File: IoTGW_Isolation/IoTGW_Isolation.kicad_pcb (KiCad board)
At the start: 4 copper layers, 40 x 48.5 mm, 33 parts, among them J1 39502-1009, J2 39502-1009, U1 TEA1-0505, U2 ISO1452BDWR, U3 LTV-817S, U4 LTV-817S, U5 LTV-817S, U6 LTV-817S, U7 LTV-817S, U8 LTV-817S

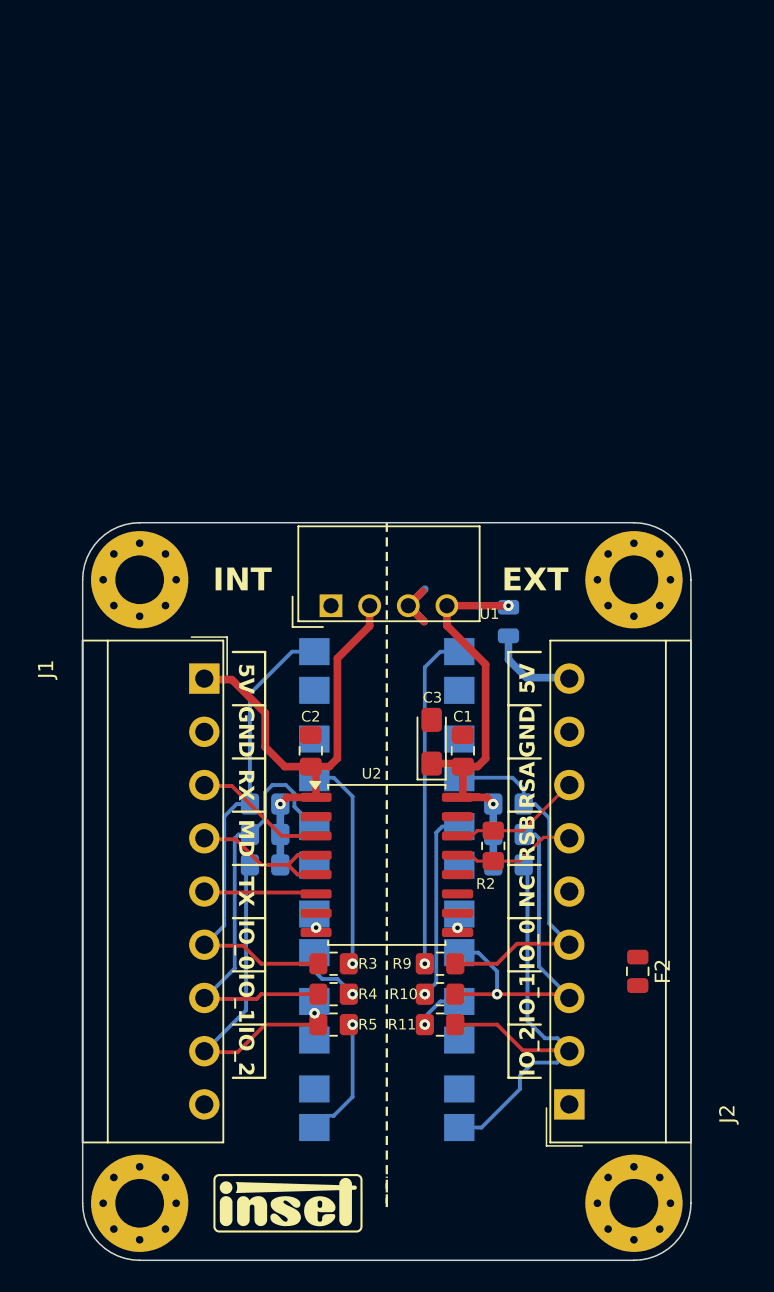
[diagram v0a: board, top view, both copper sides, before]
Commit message: 3,3V logic update
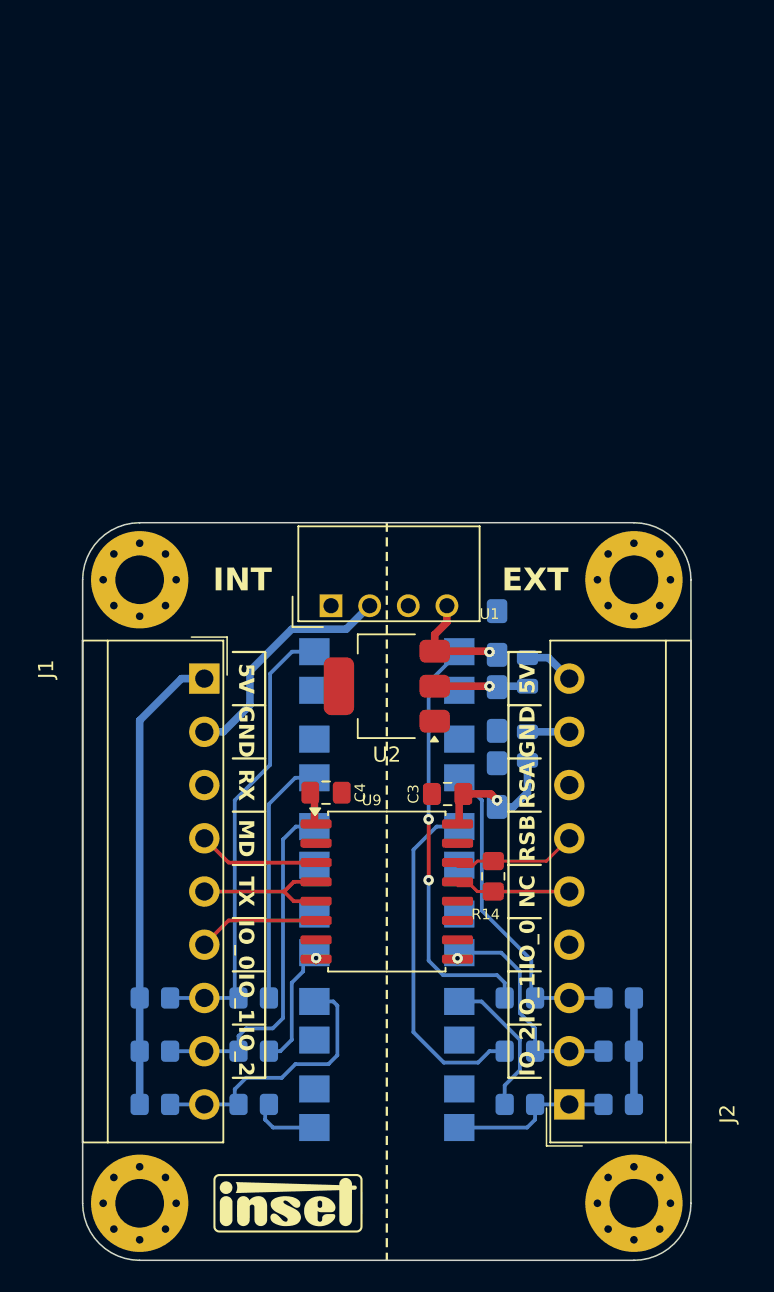
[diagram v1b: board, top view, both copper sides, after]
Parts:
- added C1: 10uF, Capacitor_Tantalum_SMD:CP_EIA-3216-18_Kemet-A_Pad1.58x1.35mm_HandSolder, B.Cu at (152.2, 97.2)
- added C2: 10uF, Capacitor_Tantalum_SMD:CP_EIA-3216-18_Kemet-A_Pad1.58x1.35mm_HandSolder, B.Cu at (152.2, 102.2)
- added U2: NCP1117-3.3, Package_TO_SOT_SMD:SOT-223-3_TabPin2, F.Cu at (145.0, 100.8)
- C5: renamed from C3; moved to B.Cu
- F2: moved to B.Cu
- R10: renamed from R11; moved to B.Cu
- R2: renamed from R3; moved to B.Cu
- R3: renamed from R4; moved to B.Cu
- R4: renamed from R5; moved to B.Cu
- R8: renamed from R9; moved to B.Cu
- R9: renamed from R10; moved to B.Cu
- moved R13 17.3 mm to (129.8, 128.2), turned to 180 degrees
- moved R7 17.3 mm to (160.2, 128.2), turned to 0 degrees
- moved F2 16.5 mm to (154.2, 104.7), turned to 90 degrees
- moved R12 16.0 mm to (129.8, 124.8), turned to 180 degrees
- moved R6 16.0 mm to (160.2, 124.8), turned to 0 degrees
- moved R11 14.7 mm to (129.8, 121.2), turned to 180 degrees
- moved R5 14.7 mm to (160.2, 121.2), turned to 0 degrees
- moved R10 7.42 mm to (153.8, 128.2)
- moved R4 7.42 mm to (136.2, 128.2)
- moved R3 6.45 mm to (136.2, 124.8)
- moved R9 6.45 mm to (153.8, 124.8)
- moved R2 5.71 mm to (136.2, 121.2)
- moved R8 5.71 mm to (153.8, 121.2)
- moved C5 5.16 mm to (152.2, 107.2)
- moved F1 3.54 mm to (154.2, 99.8), turned to 90 degrees
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- renumbered C1 to C3, C2 to C4, R12 to R11, R13 to R12, R14 to R13, R2 to R14, R6 to R5, R7 to R6, R8 to R7, U2 to U9
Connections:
- C4 pad 1: +5V -> +3.3V
- F1 pad 1: +5V_OUT -> +3.3V_OUT
- F1 pad 2: 5V_CONN -> 3.3V_CONN
- J2 pad 1: 3.3V_CONN -> GPIO_EXT_2
- J2 pad 2: 5V_CONN -> GPIO_EXT_1
- J2 pad 3: GND_OUT -> GPIO_EXT_0
- J2 pad 4: RS-485_+ -> unconnected-(J2-Pin_4-Pad4)
- J2 pad 6: unconnected-(J2-Pin_6-Pad6) -> RS-485_+
- J2 pad 7: GPIO_EXT_0 -> GND_OUT
- J2 pad 8: GPIO_EXT_1 -> 5V_CONN
- J2 pad 9: GPIO_EXT_2 -> 3.3V_CONN
- R11 pad 2: +5V -> +3.3V
- R12 pad 2: +5V -> +3.3V
- R13 pad 2: +5V -> +3.3V
- R5 pad 2: +5V_OUT -> +3.3V_OUT
- R6 pad 2: +5V_OUT -> +3.3V_OUT
- R7 pad 2: +5V_OUT -> +3.3V_OUT
- U9 pad 1: +5V -> +3.3V
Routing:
- net +3.3V: track 0.00 -> 32.6 mm
- net GPIO_EXT_2: track 32.0 -> 10.7 mm
- net +5V: track 32.3 -> 15.6 mm, vias 1 -> 0
- net +3.3V_OUT: track 0.00 -> 13.1 mm, vias 0 -> 1
- net +5V_OUT: track 28.6 -> 16.0 mm
- net Net-(R9-Pad1): track 12.6 -> 22.8 mm, vias 1 -> 0
- net GPIO_EXT_1: track 24.2 -> 14.7 mm, vias 1 -> 0
- net Net-(R10-Pad1): track 3.19 -> 9.69 mm, vias 1 -> 0
- net GPIO_OPTO_1: track 28.6 -> 22.6 mm
- net GND_OUT: track 6.15 -> 0.31 mm
- net Net-(R8-Pad1): track 22.2 -> 27.8 mm, vias 1 -> 2
- net GPIO_OPTO_2: track 22.3 -> 17.8 mm, vias 1 -> 0
- net Net-(R4-Pad1): track 8.10 -> 4.20 mm, vias 1 -> 0
- net Net-(R3-Pad1): track 4.36 -> 8.16 mm, vias 1 -> 0
- net 3.3V_CONN: track 0.00 -> 3.32 mm
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
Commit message: 3v3 update
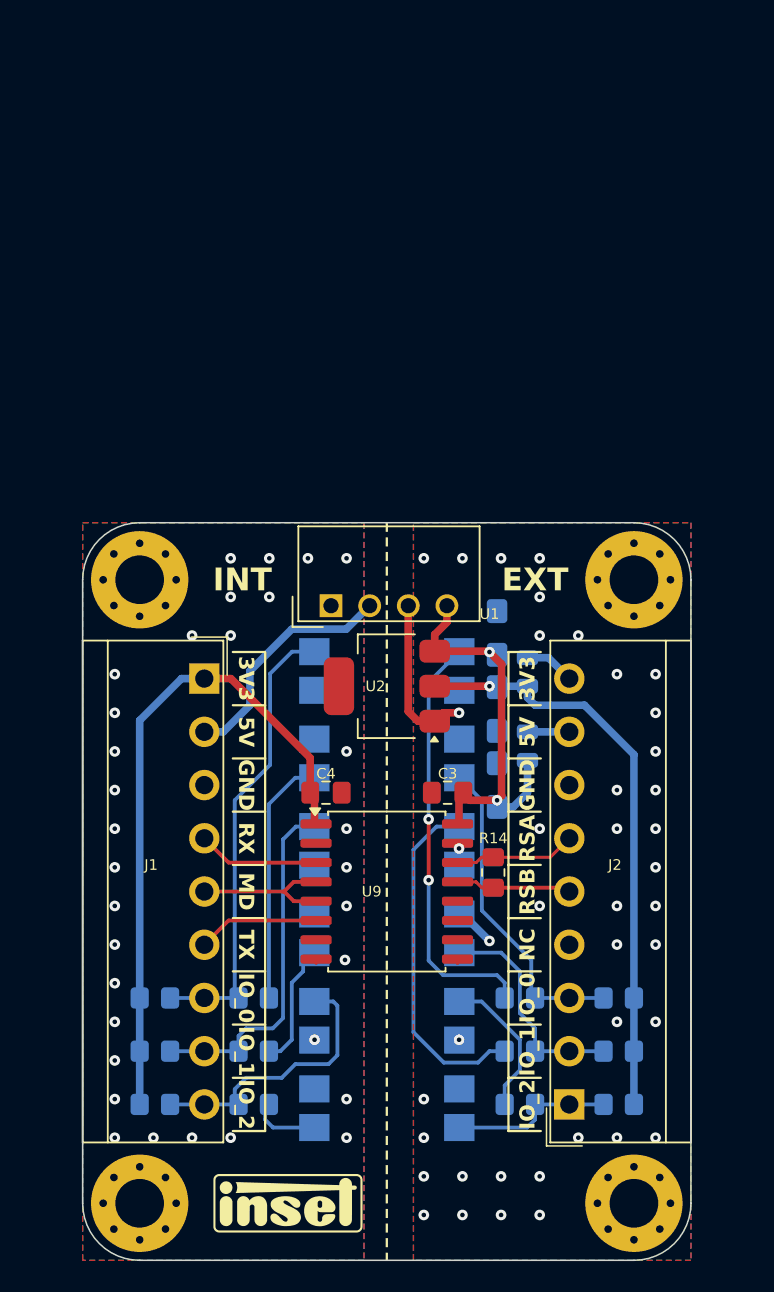
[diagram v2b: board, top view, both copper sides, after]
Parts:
- moved R14 0.25 mm to (152.0, 113.0)
- moved C3 0.09 mm to (149.0, 107.8)
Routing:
- net +3.3V_OUT: track 13.1 -> 38.4 mm
- net GND_OUT: track 0.31 -> 15.0 mm, vias 1 -> 41
- net +3.3V: track 32.6 -> 44.0 mm
- net +5V_OUT: track 16.0 -> 26.2 mm
- net GND: track 0.32 -> 0.28 mm, vias 1 -> 32
- added copper zone on B.Cu, net GND
- added copper zone on F.Cu, net GND
- added copper zone on B.Cu, net GND_OUT
- added copper zone on F.Cu, net GND_OUT
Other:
- board text added: "3V3"

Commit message: bom update
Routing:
- net GND_OUT: vias 41 -> 4
- net GND: vias 32 -> 2

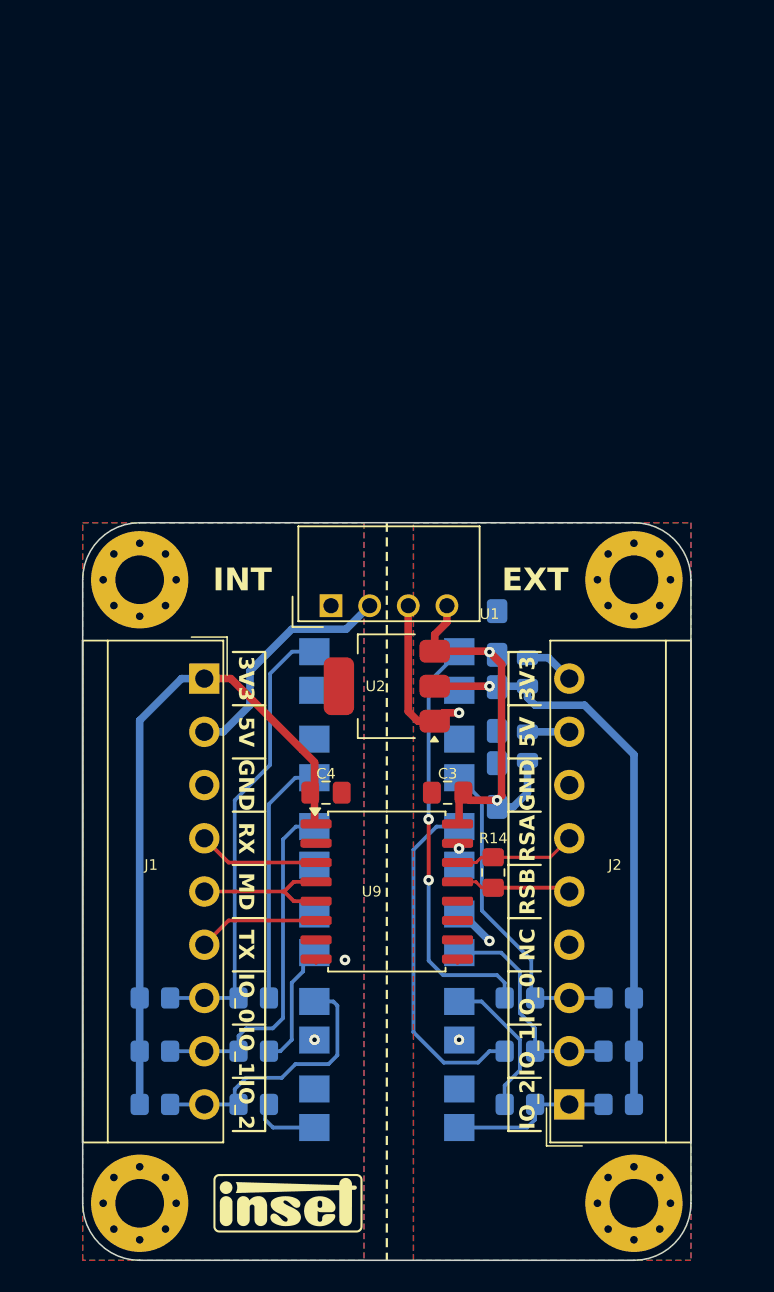
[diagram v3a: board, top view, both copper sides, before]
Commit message: FInal PCB, plot, dimensions, 3D step file
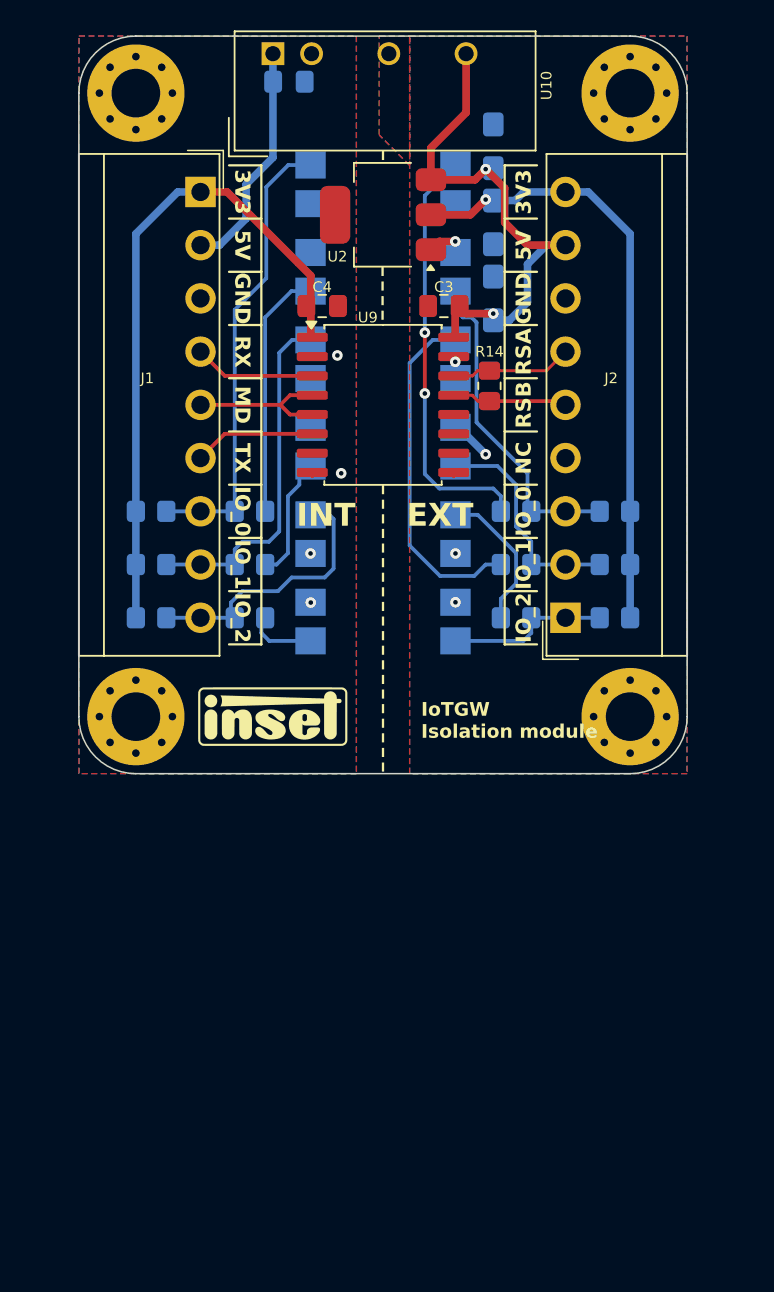
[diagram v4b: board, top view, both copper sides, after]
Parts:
- removed F1, F2: Polyfuse, Fuse:Fuse_0805_2012Metric
- removed U1: TEA1-0505, Converter_DCDC:Converter_DCDC_TRACO_TEA1-xxxx_THT
- added C6: 22uF, Capacitor_SMD:C_0805_2012Metric_Pad1.18x1.45mm_HandSolder, B.Cu at (138.6, 61.0)
- added U10: TBA2-0511, Converter_DCDC:Converter_DCDC_TRACO_TBA2-xxxx_Single_THT, F.Cu at (137.5, 59.2)
- R10, R2, R3, R4, R8, R9: value 200R -> 120R
- moved TP1 32.0 mm to (137.5, 102.8)
- moved C1 32.0 mm to (152.0, 65.2)
- moved C2 32.0 mm to (152.0, 70.2)
- moved C3 32.0 mm to (148.8, 75.8)
- moved C4 32.0 mm to (140.8, 75.8)
- moved C5 32.0 mm to (152.0, 75.2)
- moved H1 32.0 mm to (128.5, 61.8)
- moved H2 32.0 mm to (128.5, 102.8)
- moved H3 32.0 mm to (161.0, 61.8)
- moved H4 32.0 mm to (161.0, 102.8)
- moved J1 32.0 mm to (124.9, 65.8)
- moved R10 32.0 mm to (153.5, 96.2)
- moved R11 32.0 mm to (129.5, 89.2)
- moved R12 32.0 mm to (129.5, 92.8)
- moved R13 32.0 mm to (129.5, 96.2)
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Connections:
- J2 pad 8: 5V_CONN -> +5V_OUT
- J2 pad 9: 3.3V_CONN -> +3.3V_OUT
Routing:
- net GND_OUT: track 15.0 -> 5.97 mm, vias 4 -> 5
- net +5V_OUT: track 26.2 -> 34.6 mm
- net 3.3V_CONN: track 3.32 -> 0.00 mm
- net 5V_CONN: track 2.75 -> 0.00 mm
- net +3.3V_OUT: track 38.4 -> 40.2 mm
- net GND: track 0.28 -> 0.25 mm, vias 2 -> 4
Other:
- copper layers 4 -> 2
- board text added: "0"
- board text added: "0 mm"
- board text added: "0,01 mm"
- board text added: "0,02"
- board text added: "0,035 mm"
- board text added: "0,1000 mm"
- board text added: "0,1600 mm / 0,2000 mm"
- board text added: "0,7mm Pad / 0,3mm Hole"
- board text added: "1"
- board text added: "1,51 mm"
- board text added: "1,6000 mm"
- board text added: "3,3"
- board text added: "4,5"
- board text added: "40,0000 mm x 48,5000 mm"
- board text added: "B.Cu"
- board text added: "B.Mask"
- board text added: "B.Paste"
- board text added: "B.Silkscreen"
- board text added: "Bottom Silk Screen"
- board text added: "Bottom Solder Mask"
- board text added: "Bottom Solder Paste"
- board text added: "Color"
- board text added: "Dielectric 1"
- board text added: "Epsilon R"
- board text added: "F.Cu"
- board text added: "F.Mask"
- board text added: "F.Paste"
- board text added: "F.Silkscreen"
- board text added: "FR4"
- board text added: "FR4 natural"
- board text added: "IoTGW Isolation module"
- board text added: "Layer Name"
- board text added: "Loss Tangent"
- board text added: "M3"
- board text added: "Material"
- board text added: "Not specified"
- board text added: "Thickness (mm)"
- board text added: "Top Silk Screen"
- board text added: "Top Solder Mask"
- board text added: "Top Solder Paste"
- board text added: "Type"
- board text added: "Via size:"
- board text added: "copper"
- board text added: "core"
- board text removed: "0.0900 mm / 0.0900 mm"
- board text removed: "0.1000 mm"
- board text removed: "1.6000 mm"
- board text removed: "40.0000 mm x 45.0000 mm"
